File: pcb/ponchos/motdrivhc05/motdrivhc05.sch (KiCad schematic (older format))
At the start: 12 parts

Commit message: En proceso esquemático...
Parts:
- added C?: 100uf-6v, symbol CP1_Small
- added C?: 100nf, symbol CP1_Small
- added C?: 47uf-50v, symbol CP1_Small
- added D? (x2): 1N5819, symbol D_Schottky_Small
- added J?: CONN_01X02, symbol CONN_01X02
- added Q? (x2): TIP31, symbol Q_NPN_BCE
- added R? (x2): 1K, symbol R_Small
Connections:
- net +5V: now also C?.1
- net GND: now also C?.2, C?.2, C?.2, D?.2 (A), D?.2 (A), Q?.3 (E), Q?.3 (E)
- net VCC: now also C?.1
- net M4A: now reaches SH?.2
- net M4A: now also U?.15 (4A)
- net M3A: now reaches SH?.3 ((*)_3)
- net M3A: now also U?.10 (3A)
- net M2A: now reaches SH?.4
- net M2A: now also U?.7 (2A)
- net ME34: now reaches SH?.5 ((*)_5)
- net ME34: now also U?.9 (EN3,4)
- net ME12: now reaches SH?.6 ((*)_6)
- net ME12: now also U?.1 (EN1,2)
- net M1A: now reaches SH?.7
- net M1A: now also U?.2 (1A)
- new net: Q?.1 (B), R?.1 (x2)
- new net: D?.1 (K), J?.1 (P1), Q?.2 (C)
- new net: J?.2 (P2), Q?.2 (C)
- new net T1: R?.2
- new net T2: R?.2
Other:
- moved on the sheet: D?, J?, SH?, U?

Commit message: En proceso...
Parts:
- removed D? (x6): 1N5819, symbol D_Schottky_Small
- added D? (x6): 1N5819, symbol D_Schottky_Small
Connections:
- net GND: now also D?.2 (A), D?.2 (A)
- net M1A: now also SH?.8; no longer SH?.7
- net M2A: now also SH?.11 ((*/MOSI)_11); no longer SH?.4
- net M3A: now also SH?.12 ((MISO)_12); no longer SH?.3 ((*)_3)
- net M4A: now also SH?.13 ((SCK)_13); no longer SH?.2
- net ME12: now also SH?.9 ((*)_9); no longer SH?.6 ((*)_6)
- net ME34: now also SH?.10 ((*)_10); no longer SH?.5 ((*)_5)
- net T1: now also SH?.A5/2 (2/(SCL)A5)
- net T2: now also SH?.A4/2 (2/(SDA)A4)
- net VCC: now also D?.1 (K), D?.1 (K), D?.1 (K), D?.1 (K)
- net at D?.1 (K), J?.1, U?.3 (1Y): now also D?.2 (A)
- net at D?.1 (K), J?.2, U?.6 (2Y): now also D?.2 (A)
- net at J?.3, U?.11 (3Y): now also D?.1 (K), D?.2 (A)
- net at J?.4, U?.14 (4Y): now also D?.1 (K), D?.2 (A)
- net at J?.2 (P2), Q?.2 (C): now also D?.1 (K)
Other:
- moved on the sheet: D?, J?, Q?, R?

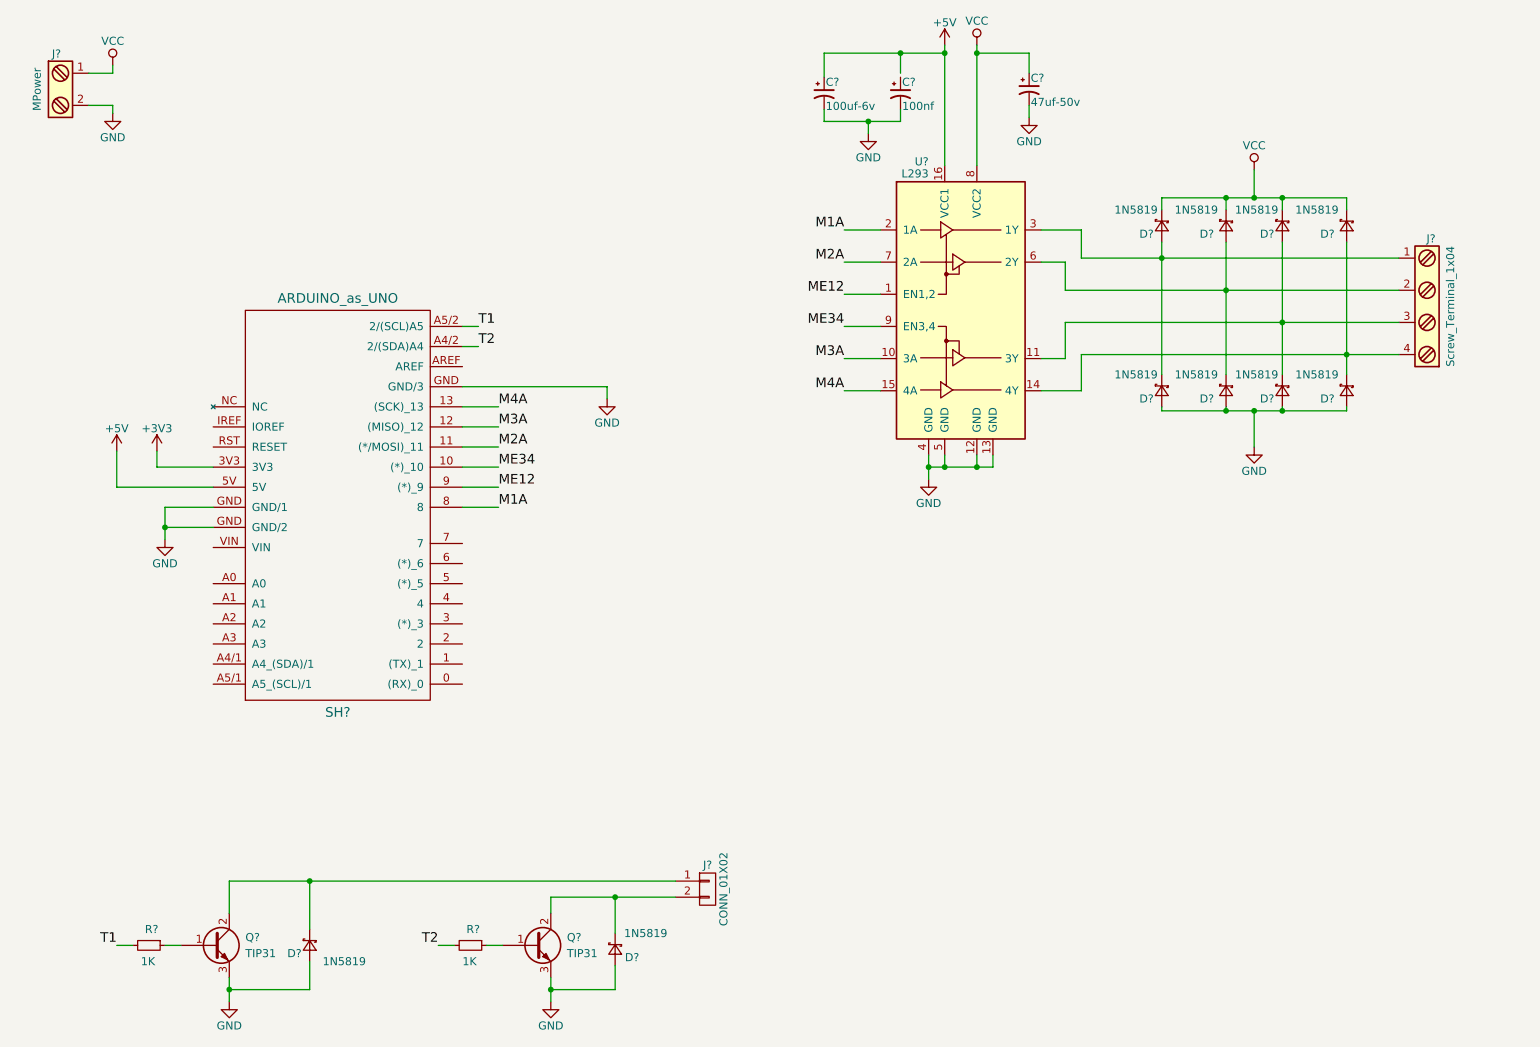
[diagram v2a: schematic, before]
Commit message: Creado componente de librería del modulo Bluetooth GW-040.
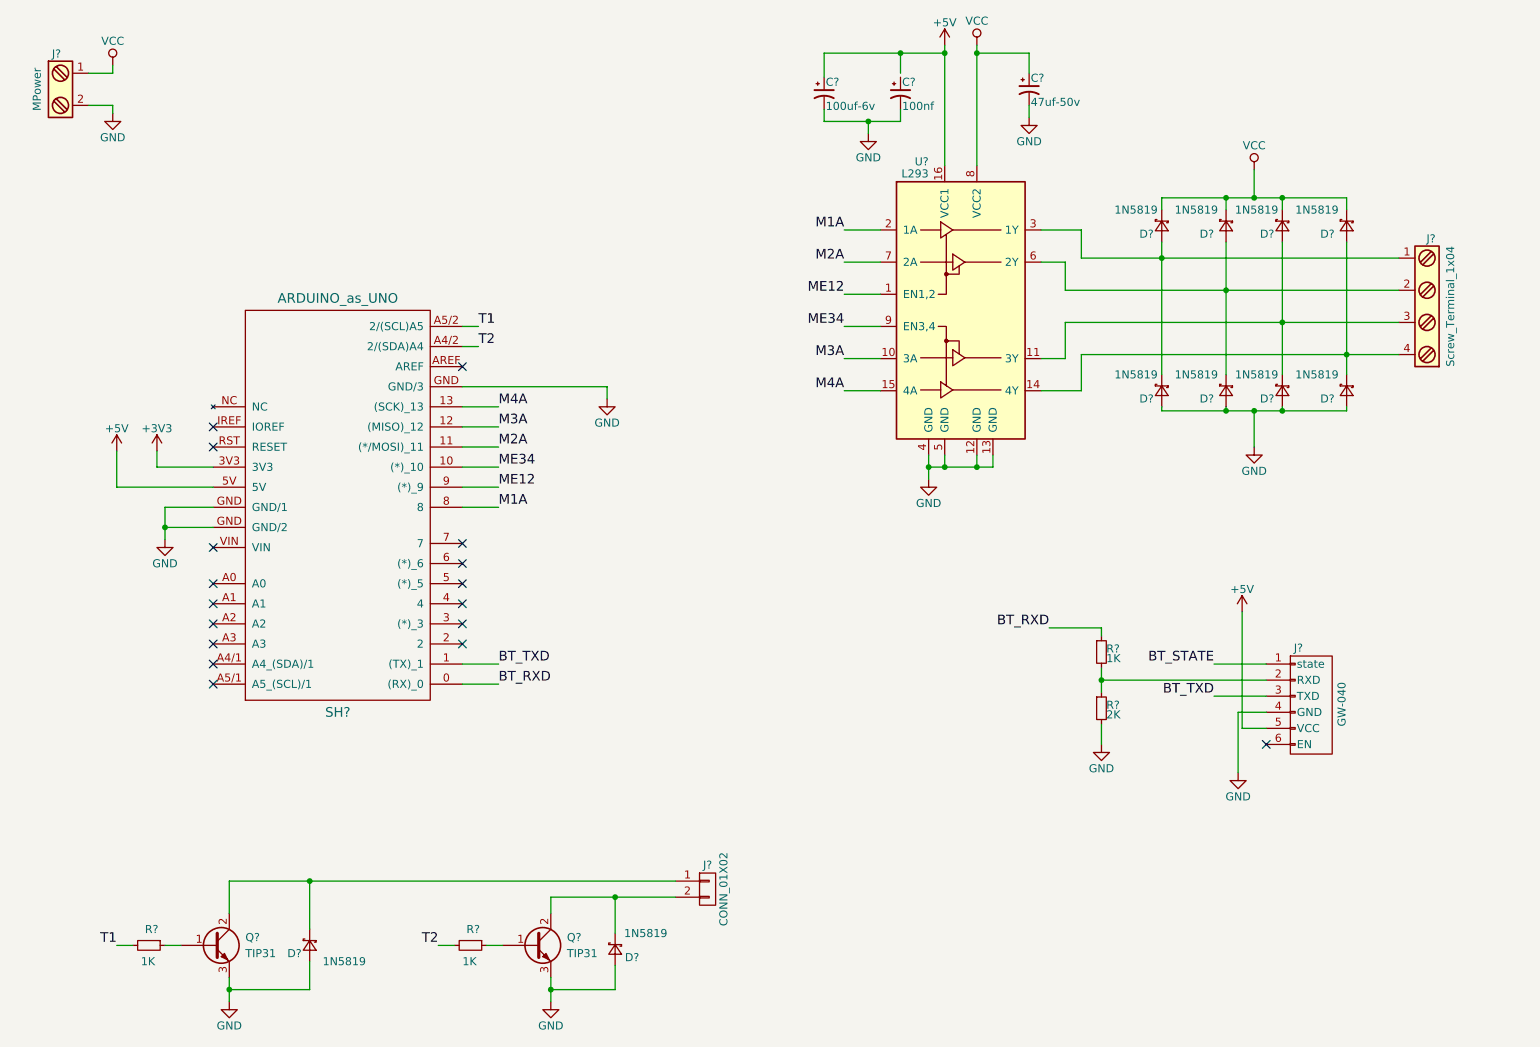
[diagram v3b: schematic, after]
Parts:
- added J?: GW-040, symbol GW-040
- added R?: 1K, symbol R_Small
- added R?: 2K, symbol R_Small
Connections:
- net +5V: now also J?.5 (VCC)
- net GND: now also J?.4 (GND), R?.2
- net BT_RXD: now reaches SH?.0 ((RX)_0)
- net BT_RXD: now also R?.1
- net BT_TXD: now reaches SH?.1 ((TX)_1)
- net BT_TXD: now also J?.3 (TXD)
- new net: J?.2 (RXD), R?.1, R?.2
- new net BT_STATE: J?.1 (state)
- no-connect marks 0 -> 17
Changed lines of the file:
@@
 LIBS:conn
 LIBS:linear
-LIBS:regul
-LIBS:74xx
-LIBS:cmos4000
-LIBS:adc-dac
-LIBS:memory
-LIBS:xilinx
-LIBS:microcontrollers
-LIBS:dsp
-LIBS:microchip
-LIBS:analog_switches
-LIBS:motorola
-LIBS:texas
-LIBS:intel
-LIBS:audio
 LIBS:interface
-LIBS:digital-audio
-LIBS:philips
-LIBS:display
-LIBS:cypress
-LIBS:siliconi
-LIBS:opto
-LIBS:atmel
 LIBS:contrib
-LIBS:valves
 LIBS:shield_arduino
 LIBS:l293
+LIBS:gw-040
 LIBS:motdrivhc05-cache
 EELAYER 25 0
@@
 	1700 1425 1700 1475
 Wire Wire Line
-	2025 3925 2025 4050
-Wire Wire Line
-	2025 4050 2025 4125
+	2025 3925 2025 4125
 Wire Wire Line
 	2325 3925 2025 3925
@@
 	4775 3175 3875 3175
 Wire Wire Line
-	6775 3600 6775 3675
-Wire Wire Line
-	6775 3675 6775 3750
+	6775 3600 6775 3750
 Wire Wire Line
 	7175 3675 7175 3600
 Wire Wire Line
-	6775 3675 6875 3675
-Wire Wire Line
-	6875 3675 7075 3675
-Wire Wire Line
-	7075 3675 7175 3675
+	6775 3675 7175 3675
 Connection ~ 6775 3675
 Wire Wire Line
@@
 Connection ~ 7075 3675
 Wire Wire Line
-	7725 2375 8225 2375
-Wire Wire Line
-	8225 2375 9700 2375
-Wire Wire Line
-	7625 2575 8625 2575
-Wire Wire Line
-	8625 2575 9700 2575
-Wire Wire Line
-	7625 2775 8975 2775
-Wire Wire Line
-	8975 2775 9700 2775
-Wire Wire Line
-	7725 2975 9375 2975
-Wire Wire Line
-	9375 2975 9700 2975
+	7725 2375 9700 2375
+Wire Wire Line
+	7625 2575 9700 2575
+Wire Wire Line
+	7625 2775 9700 2775
+Wire Wire Line
+	7725 2975 9700 2975
 Wire Wire Line
 	8225 3300 8225 3325
 Wire Wire Line
-	8225 3325 8625 3325
-Wire Wire Line
-	8625 3325 8800 3325
-Wire Wire Line
-	8800 3325 8975 3325
-Wire Wire Line
-	8975 3325 9375 3325
+	8225 3325 9375 3325
 Wire Wire Line
 	8625 3325 8625 3300
@@
 $EndComp
 Wire Wire Line
-	7075 1050 7075 1100
-Wire Wire Line
-	7075 1100 7075 1800
+	7075 1050 7075 1800
 $Comp
 L +5V #PWR?
@@
 $EndComp
 Wire Wire Line
-	6875 1050 6875 1100
-Wire Wire Line
-	6875 1100 6875 1800
+	6875 1050 6875 1800
 Text Label 6250 2200 2    60   ~ 0
 M1A
@@
 	6400 1525 6400 1600
 Wire Wire Line
-	6125 1100 6600 1100
-Wire Wire Line
-	6600 1100 6875 1100
+	6125 1100 6875 1100
 Wire Wire Line
 	6125 1100 6125 1250
@@
 	6125 1450 6125 1525
 Wire Wire Line
-	6125 1525 6400 1525
-Wire Wire Line
-	6400 1525 6600 1525
+	6125 1525 6600 1525
 Wire Wire Line
 	6600 1525 6600 1450
@@
 $EndComp
 Wire Wire Line
-	2425 6850 2425 6925
-Wire Wire Line
-	2425 6925 2425 7000
+	2425 6850 2425 7000
 $Comp
 L Q_NPN_BCE Q?
@@
 $EndComp
 Wire Wire Line
-	4425 6850 4425 6925
-Wire Wire Line
-	4425 6925 4425 7000
+	4425 6850 4425 7000
 Text Label 3725 6650 2    60   ~ 0
 T2
@@
 $EndComp
 Wire Wire Line
-	2425 6250 2925 6250
-Wire Wire Line
-	2925 6250 5200 6250
+	2425 6250 5200 6250
 Wire Wire Line
 	2425 6250 2425 6450
 Wire Wire Line
-	4425 6350 4825 6350
-Wire Wire Line
-	4825 6350 5200 6350
+	4425 6350 5200 6350
 Wire Wire Line
 	4425 6350 4425 6450
@@
 $EndComp
 Wire Wire Line
-	8225 2000 8625 2000
-Wire Wire Line
-	8625 2000 8800 2000
-Wire Wire Line
-	8800 2000 8975 2000
-Wire Wire Line
-	8975 2000 9375 2000
+	8225 2000 9375 2000
 Wire Wire Line
 	9375 2000 9375 2075
@@
 Connection ~ 8975 2000
 Wire Wire Line
-	8225 2275 8225 2375
-Wire Wire Line
-	8225 2375 8225 3100
-Wire Wire Line
-	8625 3100 8625 2575
-Wire Wire Line
-	8625 2575 8625 2275
-Wire Wire Line
-	8975 3100 8975 2775
-Wire Wire Line
-	8975 2775 8975 2275
-Wire Wire Line
-	9375 2275 9375 2975
-Wire Wire Line
-	9375 2975 9375 3100
+	8225 2275 8225 3100
+Wire Wire Line
+	8625 2275 8625 3100
+Wire Wire Line
+	8975 2275 8975 3100
+Wire Wire Line
+	9375 2275 9375 3100
 Wire Wire Line
 	8800 1825 8800 2000
@@
 Connection ~ 8975 2775
 Connection ~ 9375 2975
+$Comp
+L GW-040 J?
+U 1 1 59A4BBE6
+P 9075 5150
+F 0 "J?" H 9075 5500 50  0000 C CNN
+F 1 "GW-040" V 9345 5150 50  0000 C CNN
+F 2 "" H 9075 5150 50  0001 C CNN
+F 3 "" H 9075 5150 50  0001 C CNN
+	1    9075 5150
+	1    0    0    -1
+$EndComp
+$Comp
+L R_Small R?
+U 1 1 59A4BF57
+P 7850 4825
+F 0 "R?" H 7880 4845 50  0000 L CNN
+F 1 "1K" H 7880 4785 50  0000 L CNN
+F 2 "" H 7850 4825 50  0001 C CNN
+F 3 "" H 7850 4825 50  0001 C CNN
+	1    7850 4825
+	1    0    0    -1
+$EndComp
+$Comp
+L R_Small R?
+U 1 1 59A4C0FC
+P 7850 5175
+F 0 "R?" H 7880 5195 50  0000 L CNN
+F 1 "2K" H 7880 5135 50  0000 L CNN
+F 2 "" H 7850 5175 50  0001 C CNN
+F 3 "" H 7850 5175 50  0001 C CNN
+	1    7850 5175
+	1    0    0    -1
+$EndComp
+$Comp
+L GND #PWR?
+U 1 1 59A4C1EF
+P 7850 5400
+F 0 "#PWR?" H 7850 5150 50  0001 C CNN
+F 1 "GND" H 7850 5250 50  0000 C CNN
+F 2 "" H 7850 5400 50  0001 C CNN
+F 3 "" H 7850 5400 50  0001 C CNN
+	1    7850 5400
+	1    0    0    -1
+$EndComp
+Wire Wire Line
+	7850 4925 7850 5075
+Wire Wire Line
+	7850 5275 7850 5400
+Wire Wire Line
+	7850 4725 7850 4675
+Wire Wire Line
+	7850 4675 7525 4675
+$Comp
+L GND #PWR?
+U 1 1 59A4C3C7
+P 8700 5575
+F 0 "#PWR?" H 8700 5325 50  0001 C CNN
+F 1 "GND" H 8700 5425 50  0000 C CNN
+F 2 "" H 8700 5575 50  0001 C CNN
+F 3 "" H 8700 5575 50  0001 C CNN
+	1    8700 5575
+	1    0    0    -1
+$EndComp
+Wire Wire Line
+	8875 5200 8700 5200
+Wire Wire Line
+	8700 5200 8700 5575
+$Comp
+L +5V #PWR?
+U 1 1 59A4C522
+P 8725 4575
+F 0 "#PWR?" H 8725 4425 50  0001 C CNN
+F 1 "+5V" H 8725 4715 50  0000 C CNN
+F 2 "" H 8725 4575 50  0001 C CNN
+F 3 "" H 8725 4575 50  0001 C CNN
+	1    8725 4575
+	1    0    0    -1
+$EndComp
+Wire Wire Line
+	8725 4575 8725 5300
+Wire Wire Line
+	8725 5300 8875 5300
+Wire Wire Line
+	8875 5000 7850 5000
+Connection ~ 7850 5000
+NoConn ~ 8875 5400
+Wire Wire Line
+	8875 4900 8550 4900
+Wire Wire Line
+	8875 5100 8550 5100
+Text Label 7525 4675 2    60   ~ 0
+BT_RXD
+Text Label 8550 4900 2    60   ~ 0
+BT_STATE
+Text Label 8550 5100 2    60   ~ 0
+BT_TXD
+NoConn ~ 3875 3050
+NoConn ~ 2325 3550
+NoConn ~ 2325 3425
+NoConn ~ 2325 4175
+Wire Wire Line
+	3875 5025 4100 5025
+Text Label 4100 5025 0    60   ~ 0
+BT_RXD
+Wire Wire Line
+	3875 4900 4100 4900
+Text Label 4100 4900 0    60   ~ 0
+BT_TXD
+NoConn ~ 3875 4775
+NoConn ~ 3875 4650
+NoConn ~ 3875 4525
+NoConn ~ 3875 4400
+NoConn ~ 3875 4275
+NoConn ~ 3875 4150
+NoConn ~ 2325 4400
+NoConn ~ 2325 4525
+NoConn ~ 2325 4650
+NoConn ~ 2325 4775
+NoConn ~ 2325 4900
+NoConn ~ 2325 5025
 $EndSCHEMATC

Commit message: Correciónes del componente esquemático Arduino shield. Finalizada propuesta de esquemático. PCB en desarrollo.
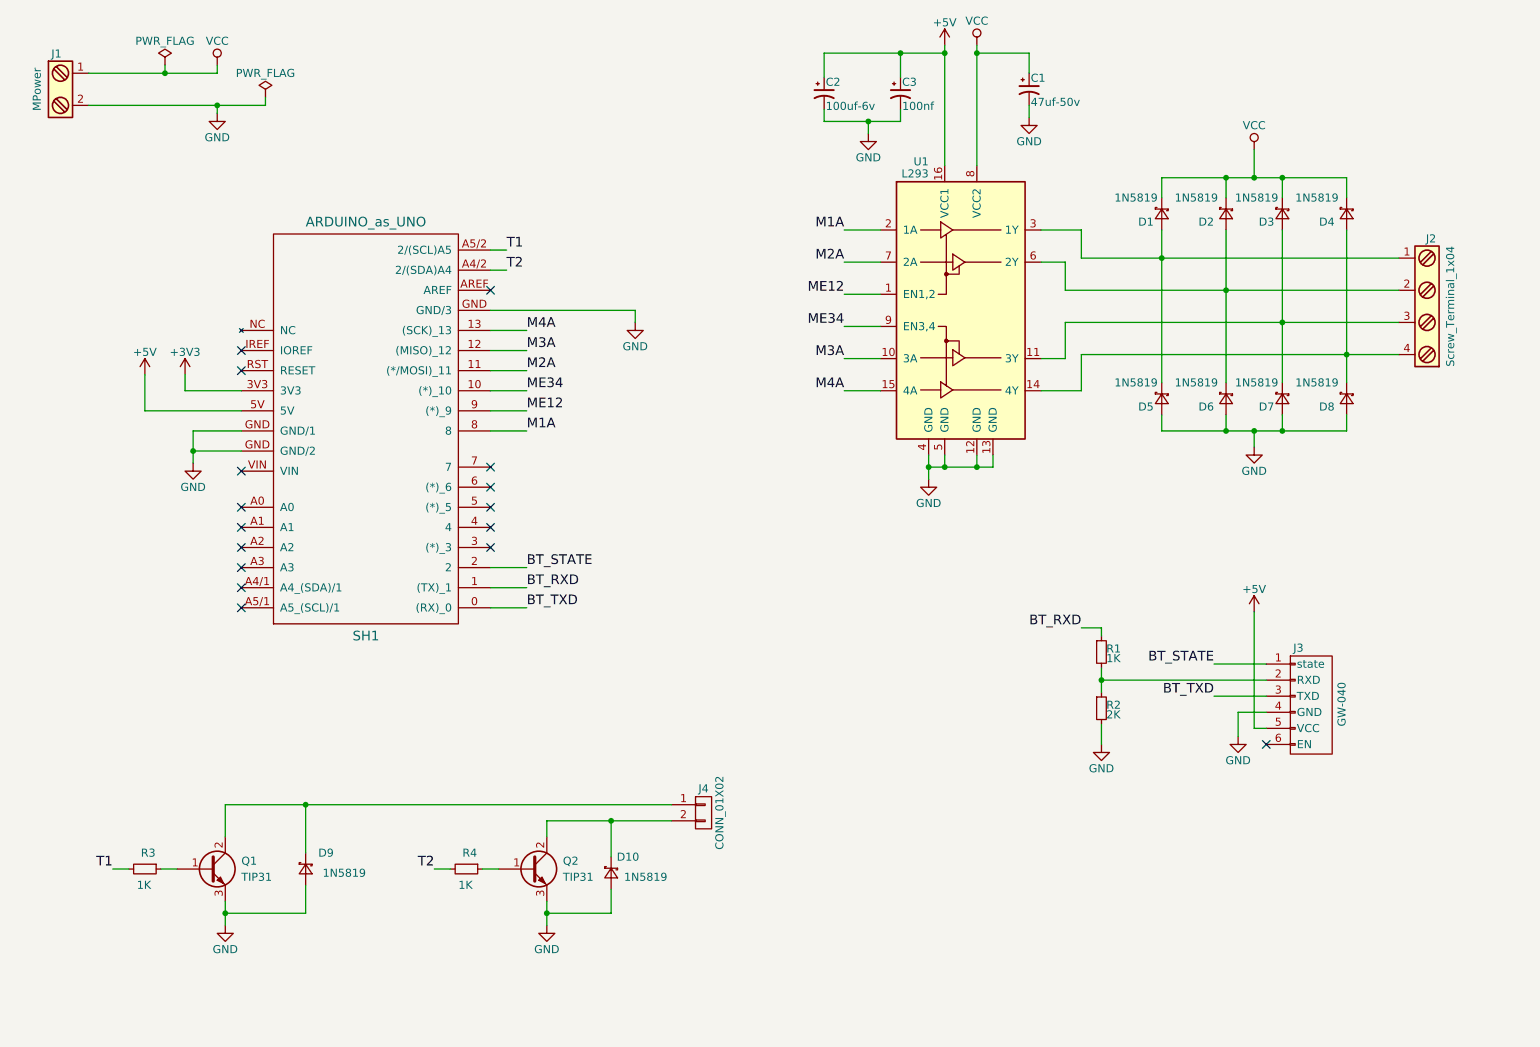
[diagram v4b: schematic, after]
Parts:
- C1, C2: renamed from C?; footprint (none) -> Capacitors_ThroughHole:C_Radial_D7.5_L11.2_P2.5
- C3: renamed from C?; footprint (none) -> Capacitors_ThroughHole:C_Disc_D3_P2.5
- D1, D10, D2, D3, D4, D5, D6, D7, D8, D9: renamed from D?; footprint (none) -> Diodes_ThroughHole:Diode_DO-41_SOD81_Horizontal_RM10
- J1: renamed from J?; footprint (none) -> Connect:bornier2
- J2: renamed from J?; footprint (none) -> Connect:bornier4
- J3: renamed from J?; footprint (none) -> Socket_Strips:Socket_Strip_Angled_1x06
- J4: renamed from J?; footprint (none) -> Pin_Headers:Pin_Header_Straight_1x02
- Q1, Q2: renamed from Q?; footprint (none) -> TO_SOT_Packages_THT:TO-220_Neutral123_Horizontal_LargePads
- R1, R2, R3, R4: renamed from R?; footprint (none) -> Resistors_ThroughHole:Resistor_Horizontal_RM10mm
- SH1: renamed from SH?; footprint (none) -> Arduino_Uno:ARDUINO_as_UNO_R3_CONTOUR_ELL
- gave numbers to parts that had none: 1
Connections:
- net +5V: now also C3.1
- net BT_RXD: now also SH1.1 ((TX)_1); no longer SH1.0 ((RX)_0)
- net BT_STATE: now also SH1.2
- net BT_TXD: now also SH1.0 ((RX)_0); no longer SH1.1 ((TX)_1)
- no-connect marks 17 -> 16
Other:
- moved on the sheet: D1, D10, D2, D3, D4, D5, D6, D7, D8, D9, J4, Q1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

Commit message: Haciendo PCB...
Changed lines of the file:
@@
 Connection ~ 7075 3675
 Wire Wire Line
-	7725 2375 9700 2375
+	7700 2375 9700 2375
 Wire Wire Line
 	7625 2575 9700 2575
@@
 	7625 2775 9700 2775
 Wire Wire Line
-	7725 2975 9700 2975
+	7700 2975 9700 2975
 Wire Wire Line
 	8225 3350 8225 3450
@@
 Wire Wire Line
 	4050 2450 4150 2450
-Wire Wire Line
-	7625 2575 7625 2400
-Wire Wire Line
-	7625 2400 7475 2400
-Wire Wire Line
-	7725 2375 7725 2200
-Wire Wire Line
-	7725 2200 7475 2200
-Wire Wire Line
-	7625 2775 7625 3000
-Wire Wire Line
-	7625 3000 7475 3000
-Wire Wire Line
-	7475 3200 7725 3200
-Wire Wire Line
-	7725 3200 7725 2975
 $Comp
 L D_Schottky_Small D7
@@
 Wire Wire Line
 	4050 4300 4275 4300
+Wire Wire Line
+	7475 2200 7700 2200
+Wire Wire Line
+	7700 2200 7700 2375
+Wire Wire Line
+	7625 2575 7625 2400
+Wire Wire Line
+	7625 2400 7475 2400
+Wire Wire Line
+	7700 2975 7700 3200
+Wire Wire Line
+	7700 3200 7475 3200
+Wire Wire Line
+	7625 2775 7625 3000
+Wire Wire Line
+	7625 3000 7475 3000
 $EndSCHEMATC

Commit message: En desarrollo...
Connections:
- net T1: now also SH1.A4/2 (2/(SDA)A4); no longer SH1.A5/2 (2/(SCL)A5)
- net T2: now also SH1.A5/2 (2/(SCL)A5); no longer SH1.A4/2 (2/(SDA)A4)
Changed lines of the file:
@@
 	2900 6450 2400 6450
 Connection ~ 2400 6450
-Text Label 4150 2325 0    60   ~ 0
+Text Label 4150 2450 0    60   ~ 0
 T1
 Wire Wire Line
-	4050 2325 4150 2325
-Text Label 4150 2450 0    60   ~ 0
+	4050 2450 4150 2450
+Text Label 4150 2325 0    60   ~ 0
 T2
 Wire Wire Line
-	4050 2450 4150 2450
+	4050 2325 4150 2325
 $Comp
 L D_Schottky_Small D7
